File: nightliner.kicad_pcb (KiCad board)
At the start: 2 copper layers, 154.8 x 116.1 mm, 83 parts, among them J1 TYPE-C-31-M-12, J2 Battery, J4 Serial, P1 ISP_Prog, SW1 pinky_top, SW10 inner_home, SW11 pinky_bottom, SW12 ring_bottom, SW13 middle_bottom, SW14 index_bottom, SW15 inner_bottom, SW16 outer_top, SW17 outer_home, SW18 near_thumb, SW19 home_thumb, SW2 ring_top, SW20 far_thumb, SW21 ON_OFF, SW22 RESET, SW3 middle_top, SW4 index_top, SW5 inner_top, SW6 pinky_home, SW7 ring_home, SW8 middle_home, SW9 index_home, U1 holyiot-18010, U2 TVS2200DRV, U3 USBLC6-2SC6, U4 BQ24075RGT, U5 XC6220B331MR

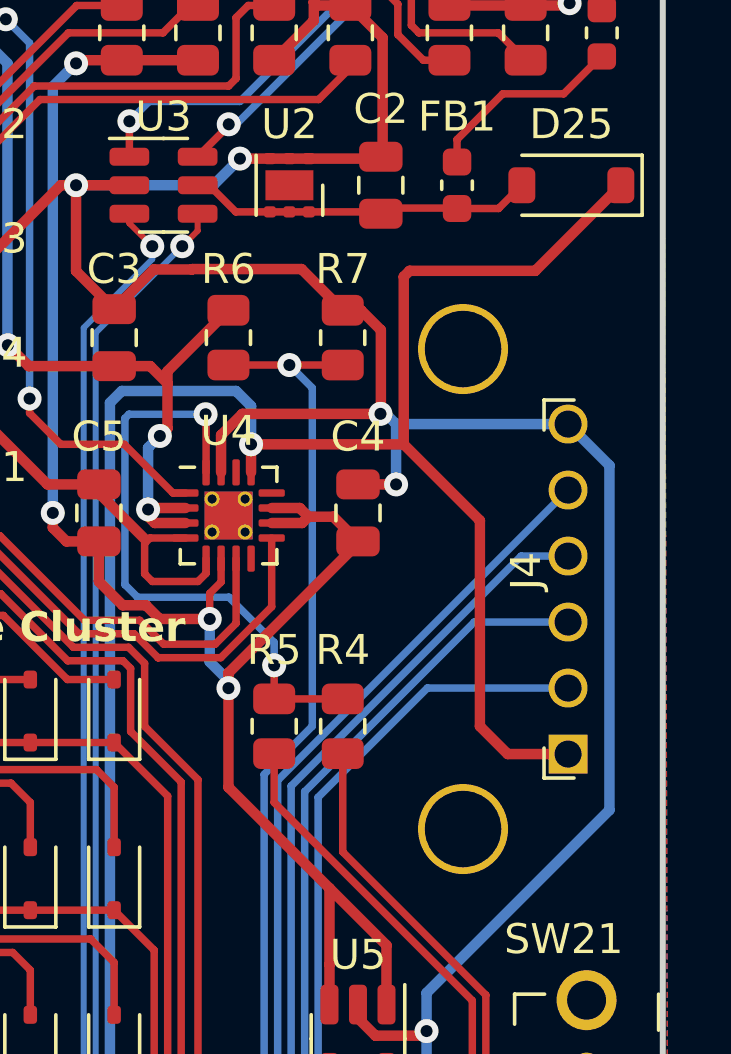
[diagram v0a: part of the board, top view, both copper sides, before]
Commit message: fix: move mag connector up, preserve wall thickness of case
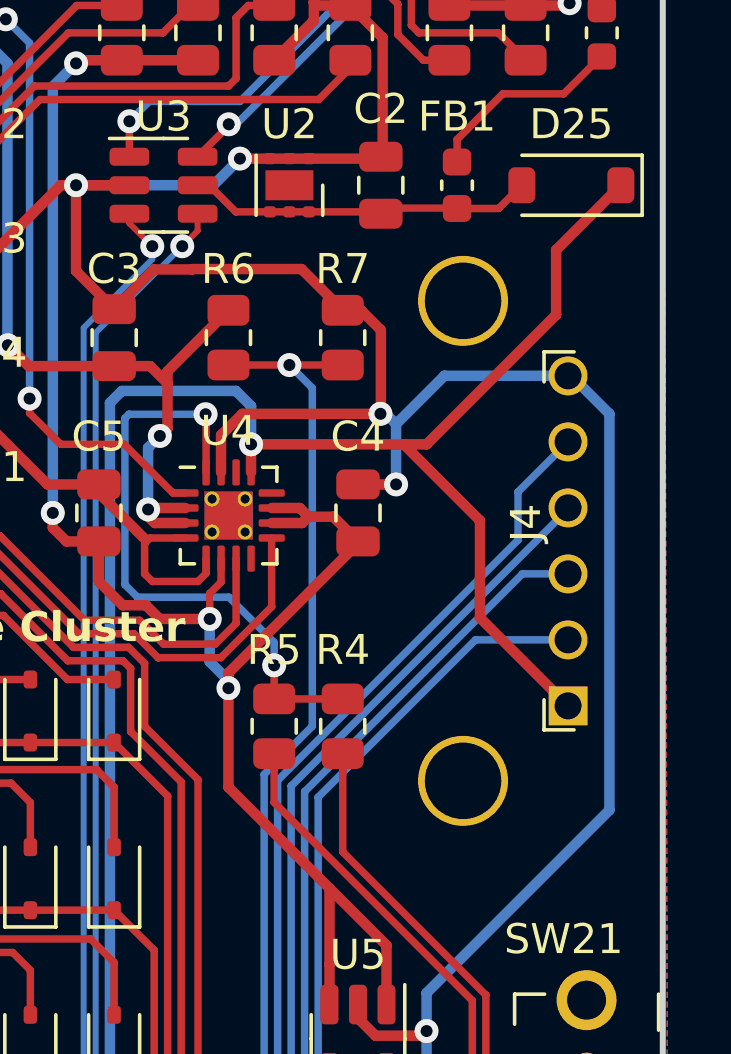
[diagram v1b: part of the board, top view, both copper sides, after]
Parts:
- moved J4 1.61 mm to (170.3, 72.7)
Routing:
- net VBUS: track 84.2 -> 79.4 mm
- net GND: track 197.3 -> 199.7 mm
- net CTS: track 35.8 -> 37.4 mm
- net RTS: track 34.1 -> 34.8 mm
- net TX: track 32.4 -> 33.0 mm
- net RX: track 30.7 -> 31.4 mm
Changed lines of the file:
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@@
   )
   (footprint "miro_keyboard:MagConn_6pin_left" (layer "F.Cu")
-    (at 170.324 74.332 90)
+    (at 170.324 72.726 90)
     (descr "Magnetic pogo pin connector, 6 pins, left angled")
     (tags "connector magnetic pgo")
@@
   (via (at 150.622 102.108) (size 0.8) (drill 0.4) (layers "F.Cu" "B.Cu") (net 2))
   (via (at 129.032 84.328) (size 0.8) (drill 0.4) (layers "F.Cu" "B.Cu") (free) (net 2))
+  (segment (start 171.704 62.992) (end 171.704 76.2) (width 0.35) (layer "B.Cu") (net 2))
+  (segment (start 165.608 82.296) (end 165.608 83.566) (width 0.35) (layer "B.Cu") (net 2))
+  (segment (start 164.592 63.332) (end 166.202 61.722) (width 0.35) (layer "B.Cu") (net 2))
   (segment (start 165.608 89.916) (end 165.608 83.566) (width 0.35) (layer "B.Cu") (net 2))
   (segment (start 159.3865 54.4845) (end 158.499 55.372) (width 0.35) (layer "B.Cu") (net 2))
+  (segment (start 166.202 61.722) (end 170.238001 61.722) (width 0.35) (layer "B.Cu") (net 2))
   (segment (start 150.622 102.108) (end 150.622 96.454) (width 0.35) (layer "B.Cu") (net 2))
   (segment (start 170.3755 49.302905) (end 170.3755 48.7095) (width 0.35) (layer "B.Cu") (net 2))
   (segment (start 164.0715 62.992) (end 164.252 62.992) (width 0.35) (layer "B.Cu") (net 2))
-  (segment (start 171.704 76.2) (end 165.608 82.296) (width 0.35) (layer "B.Cu") (net 2))
+  (segment (start 170.336001 61.624) (end 171.704 62.992) (width 0.35) (layer "B.Cu") (net 2))
+  (segment (start 170.238001 61.722) (end 170.336001 61.624) (width 0.35) (layer "B.Cu") (net 2))
   (segment (start 164.252 62.992) (end 164.592 63.332) (width 0.35) (layer "B.Cu") (net 2))
   (segment (start 170.3755 48.7095) (end 168.8975 47.2315) (width 0.35) (layer "B.Cu") (net 2))
-  (segment (start 171.704 64.712) (end 171.704 76.2) (width 0.35) (layer "B.Cu") (net 2))
-  (segment (start 170.324 63.332) (end 171.704 64.712) (width 0.35) (layer "B.Cu") (net 2))
   (segment (start 158.499 55.372) (end 153.924 55.372) (width 0.35) (layer "B.Cu") (net 2))
   (segment (start 168.8975 47.2315) (end 168.402 47.2315) (width 0.35) (layer "B.Cu") (net 2))
-  (segment (start 164.592 63.332) (end 170.324 63.332) (width 0.35) (layer "B.Cu") (net 2))
-  (segment (start 165.608 82.296) (end 165.608 83.566) (width 0.35) (layer "B.Cu") (net 2))
   (segment (start 164.592 65.344) (end 164.592 63.332) (width 0.35) (layer "B.Cu") (net 2))
-  (segment (start 168.312 74.332) (end 167.386 73.406) (width 0.35) (layer "F.Cu") (net 3))
+  (segment (start 171.704 76.2) (end 165.608 82.296) (width 0.35) (layer "B.Cu") (net 2))
   (segment (start 153.924 104.14) (end 153.926 104.138) (width 0.35) (layer "F.Cu") (net 3))
-  (segment (start 164.846 58.42) (end 165.042349 58.223651) (width 0.35) (layer "F.Cu") (net 3))
-  (segment (start 167.386 73.406) (end 167.386 66.548) (width 0.35) (layer "F.Cu") (net 3))
+  (segment (start 170.324 72.726) (end 167.386 69.788) (width 0.35) (layer "F.Cu") (net 3))
+  (segment (start 167.386 66.548) (end 164.846 64.008) (width 0.35) (layer "F.Cu") (net 3))
+  (segment (start 169.926 59.69) (end 169.926 57.53) (width 0.35) (layer "F.Cu") (net 3))
+  (segment (start 165.608 64.008) (end 169.926 59.69) (width 0.35) (layer "F.Cu") (net 3))
   (segment (start 153.926 104.138) (end 155.384 104.138) (width 0.35) (layer "F.Cu") (net 3))
-  (segment (start 170.324 74.332) (end 168.312 74.332) (width 0.35) (layer "F.Cu") (net 3))
+  (segment (start 164.846 64.008) (end 165.608 64.008) (width 0.35) (layer "F.Cu") (net 3))
+  (segment (start 169.926 57.53) (end 172.084 55.372) (width 0.35) (layer "F.Cu") (net 3))
   (segment (start 159.758 64.008) (end 159.758 64.943) (width 0.35) (layer "F.Cu") (net 3))
-  (segment (start 169.232349 58.223651) (end 172.084 55.372) (width 0.35) (layer "F.Cu") (net 3))
-  (segment (start 164.846 64.008) (end 164.846 58.42) (width 0.35) (layer "F.Cu") (net 3))
+  (segment (start 167.386 69.788) (end 167.386 66.548) (width 0.35) (layer "F.Cu") (net 3))
   (segment (start 159.758 64.008) (end 164.846 64.008) (width 0.35) (layer "F.Cu") (net 3))
-  (segment (start 165.042349 58.223651) (end 169.232349 58.223651) (width 0.35) (layer "F.Cu") (net 3))
-  (segment (start 167.386 66.548) (end 164.846 64.008) (width 0.35) (layer "F.Cu") (net 3))
   (via (at 153.924 104.14) (size 0.8) (drill 0.4) (layers "F.Cu" "B.Cu") (net 3))
   (via (at 159.758 64.008) (size 0.8) (drill 0.4) (layers "F.Cu" "B.Cu") (net 3))
@@
   (segment (start 158.361251 55.372) (end 157.977 55.372) (width 0.25) (layer "F.Cu") (net 67))
   (segment (start 168.009 56.147) (end 168.784 55.372) (width 0.25) (layer "F.Cu") (net 67))
-  (segment (start 165.633188 72.132) (end 170.324 72.132) (width 0.25) (layer "B.Cu") (net 68))
-  (segment (start 162.084 96.588) (end 161.994 96.498) (width 0.25) (layer "B.Cu") (net 68))
   (segment (start 161.994 96.498) (end 161.994 75.771188) (width 0.25) (layer "B.Cu") (net 68))
-  (segment (start 161.994 75.771188) (end 165.633188 72.132) (width 0.25) (layer "B.Cu") (net 68))
-  (segment (start 161.544 75.584792) (end 161.544 94.700792) (width 0.25) (layer "B.Cu") (net 69))
-  (segment (start 170.324 69.932) (end 167.196792 69.932) (width 0.25) (layer "B.Cu") (net 69))
+  (segment (start 162.084 96.588) (end 161.994 96.498) (width 0.25) (layer "B.Cu") (net 68))
+  (segment (start 167.239188 70.526) (end 170.324 70.526) (width 0.25) (layer "B.Cu") (net 68))
+  (segment (start 161.994 75.771188) (end 167.239188 70.526) (width 0.25) (layer "B.Cu") (net 68))
   (segment (start 160.984 95.260792) (end 160.984 96.588) (width 0.25) (layer "B.Cu") (net 69))
-  (segment (start 167.196792 69.932) (end 161.544 75.584792) (width 0.25) (layer "B.Cu") (net 69))
   (segment (start 161.544 94.700792) (end 160.984 95.260792) (width 0.25) (layer "B.Cu") (net 69))
-  (segment (start 161.094 75.398396) (end 161.094 94.514396) (width 0.25) (layer "B.Cu") (net 70))
-  (segment (start 170.324 67.732) (end 168.760396 67.732) (width 0.25) (layer "B.Cu") (net 70))
-  (segment (start 161.094 94.514396) (end 159.884 95.724396) (width 0.25) (layer "B.Cu") (net 70))
+  (segment (start 170.324 68.326) (end 168.802792 68.326) (width 0.25) (layer "B.Cu") (net 69))
+  (segment (start 161.544 75.584792) (end 161.544 94.700792) (width 0.25) (layer "B.Cu") (net 69))
+  (segment (start 168.802792 68.326) (end 161.544 75.584792) (width 0.25) (layer "B.Cu") (net 69))
   (segment (start 159.884 95.724396) (end 159.884 96.588) (width 0.25) (layer "B.Cu") (net 70))
-  (segment (start 168.760396 67.732) (end 161.094 75.398396) (width 0.25) (layer "B.Cu") (net 70))
+  (segment (start 161.094 94.514396) (end 159.884 95.724396) (width 0.25) (layer "B.Cu") (net 70))
+  (segment (start 161.094 75.398396) (end 161.094 94.514396) (width 0.25) (layer "B.Cu") (net 70))
+  (segment (start 170.324 66.168396) (end 161.094 75.398396) (width 0.25) (layer "B.Cu") (net 70))
+  (segment (start 170.324 66.126) (end 170.324 66.168396) (width 0.25) (layer "B.Cu") (net 70))
   (segment (start 153.074 106.338) (end 155.384 106.338) (width 0.2) (layer "F.Cu") (net 84))
   (segment (start 155.702 56.322) (end 155.702 56.642) (width 0.2) (layer "F.Cu") (net 84))
@@
   (segment (start 152.8 104.622) (end 152.8 93.129686) (width 0.2) (layer "B.Cu") (net 85))
   (segment (start 154.578 60.289503) (end 157.463503 57.404) (width 0.2) (layer "B.Cu") (net 85))
-  (segment (start 160.644 75.212) (end 170.324 65.532) (width 0.25) (layer "B.Cu") (net 98))
-  (segment (start 160.644 94.328) (end 160.644 75.212) (width 0.25) (layer "B.Cu") (net 98))
+  (segment (start 160.644 75.212) (end 168.656 67.2) (width 0.25) (layer "B.Cu") (net 98))
   (segment (start 158.784 96.588) (end 158.784 96.188) (width 0.25) (layer "B.Cu") (net 98))
+  (segment (start 160.644 94.328) (end 160.644 75.212) (width 0.25) (layer "B.Cu") (net 98))
+  (segment (start 168.656 65.594) (end 170.324 63.926) (width 0.25) (layer "B.Cu") (net 98))
   (segment (start 158.784 96.188) (end 160.644 94.328) (width 0.25) (layer "B.Cu") (net 98))
+  (segment (start 168.656 67.2) (end 168.656 65.594) (width 0.25) (layer "B.Cu") (net 98))
   (zone (net 2) (net_name "GND") (layer "F.Cu") (hatch edge 0.5)
     (priority 1)
